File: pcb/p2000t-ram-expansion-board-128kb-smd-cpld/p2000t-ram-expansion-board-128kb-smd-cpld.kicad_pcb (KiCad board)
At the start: 2 copper layers, 110 x 45.5 mm, 14 parts, among them J1 EXPANSION BOARD, J2 POWER, J3 TERMINAL, U1 ATF1502ASV-xAx44, U2 62128

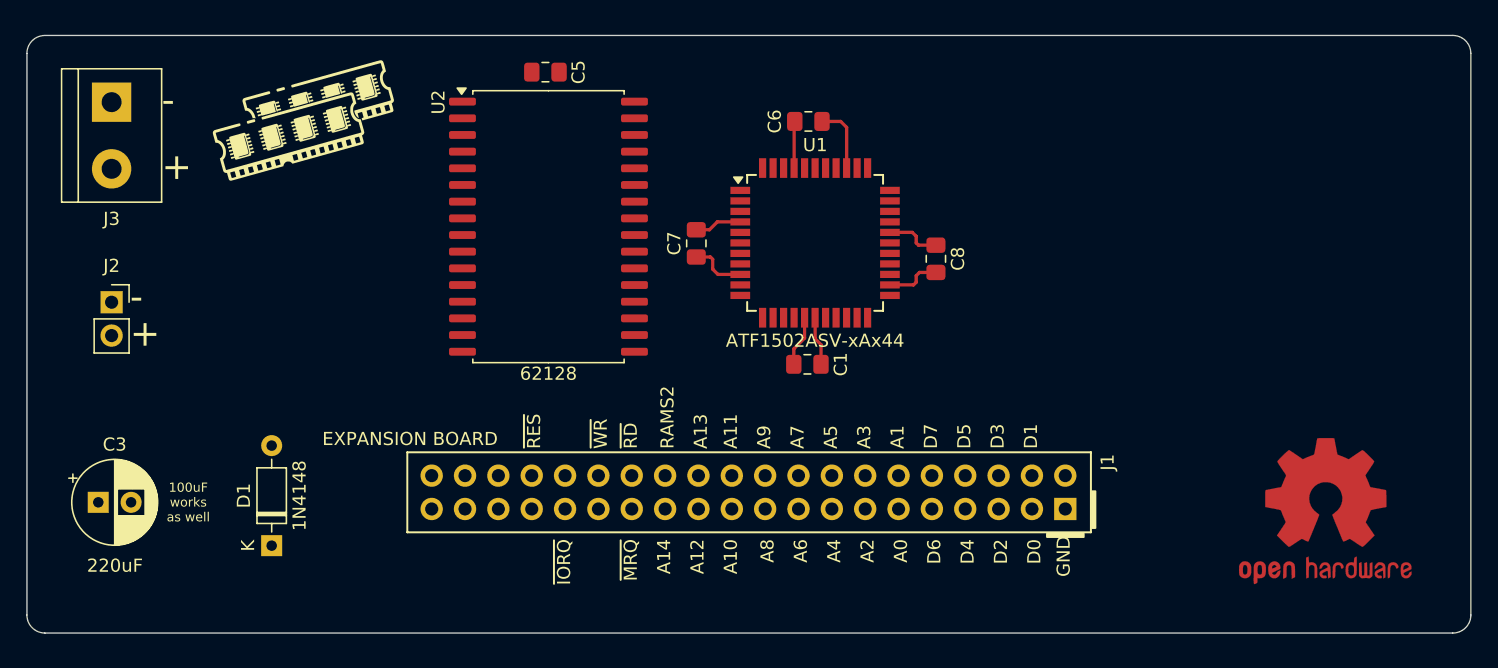
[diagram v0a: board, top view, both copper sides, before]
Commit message: Initial commit CPLD-based RAM expansion
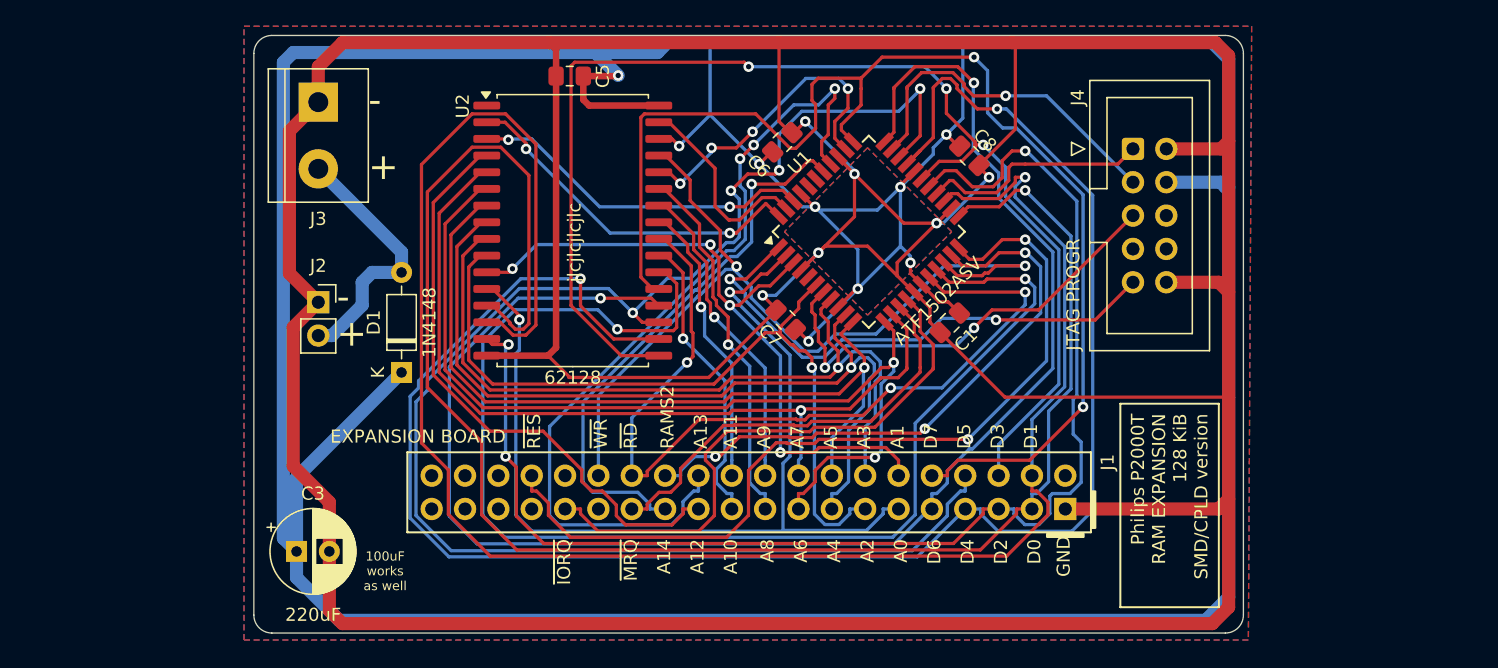
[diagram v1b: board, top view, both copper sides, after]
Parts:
- removed LOGO1: OSHW-Logo2_14.6x12mm_Copper_AND_Mask, components:OSHW-Logo2_14.6x12mm_Copper_AND_Mask
- added J4: Atmel-JTAG-10, Connector_IDC:IDC-Header_2x05_P2.54mm_Vertical, F.Cu at (104.2, 53.1)
- G***: moved to B.Cu
- U1: value ATF1502ASV-xAx44 -> ATF1502ASV
- moved G*** 20.8 mm to (61.5, 54.8), turned to 180 degrees
- moved D1 16.5 mm to (48.5, 70.1)
- moved J2 15.7 mm to (42.2, 64.8)
- moved J3 15.7 mm to (42.2, 49.5)
- moved C3 15.6 mm to (40.5, 83.8)
- moved C1 11.3 mm to (90.3, 66.3), turned to -135 degrees
- moved C7 8.96 mm to (77.8, 66.1), turned to 135 degrees
- moved C8 8.25 mm to (91.8, 53.6), turned to -45 degrees
- moved U1 4.18 mm to (84.1, 59.4), turned to 45 degrees
- moved C6 2.54 mm to (77.5, 52.6), turned to 45 degrees
- moved U2 1.87 mm to (61.5, 59.3)
- moved C5 1.87 mm to (61.3, 47.5)
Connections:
- U1 pad 1: unconnected-(U1-I/O/TDI-Pad1) -> TDI
- U1 pad 19: unconnected-(U1-I/O/PD2-Pad19) -> ~{CS1}
- U1 pad 26: unconnected-(U1-I/O/TCK-Pad26) -> TCK
- U1 pad 32: unconnected-(U1-I/O/TDO-Pad32) -> TDO
- U1 pad 35: unconnected-(U1-I/O/GCLK3-Pad35) -> R0
- U1 pad 37: unconnected-(U1-I/GCLK1-Pad37) -> A13
- U1 pad 38: unconnected-(U1-I/OE1/Vpp-Pad38) -> A14
- U1 pad 42: unconnected-(U1-I/O-Pad42) -> R1
- U1 pad 43: unconnected-(U1-I/O-Pad43) -> R2
- U1 pad 44: unconnected-(U1-I/O-Pad44) -> R3
- U1 pad 7: unconnected-(U1-I/O/TMS-Pad7) -> TMS
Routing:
- net GND: track 16.8 -> 400.2 mm, vias 0 -> 6
- net +5V: track 15.8 -> 342.9 mm, vias 0 -> 9
- net D1: track 0.00 -> 142.5 mm, vias 0 -> 1
- net D4: track 0.00 -> 140.0 mm, vias 0 -> 2
- net D0: track 0.00 -> 129.4 mm, vias 0 -> 1
- net D6: track 0.00 -> 119.5 mm, vias 0 -> 2
- net D5: track 0.00 -> 118.2 mm, vias 0 -> 4
- net D2: track 0.00 -> 100.8 mm, vias 0 -> 3
- net ~{CS1}: track 0.00 -> 98.5 mm, vias 0 -> 2
- net D3: track 0.00 -> 96.6 mm, vias 0 -> 3
- net D7: track 0.00 -> 96.1 mm, vias 0 -> 2
- net A0: track 0.00 -> 75.0 mm, vias 0 -> 2
- net A6: track 0.00 -> 72.0 mm, vias 0 -> 2
- net ~{WR}: track 0.00 -> 66.8 mm, vias 0 -> 2
- net ~{RES}: track 0.00 -> 66.1 mm, vias 0 -> 2
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- added copper zone on B.Cu, net +5V
- added copper zone on F.Cu, net GND
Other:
- board size 110 x 45.5 mm -> 75.4 x 45.5 mm
- board text added: "JTAG PROGR"
- board text added: "Philips P2000T MEMORY EXPANSION 128 KiB SMD/CPLD"
- board text added: "Philips P2000T RAM EXPANSION 128 KiB SMD/CPLD version"
- board text added: "https://github.com/ifilot/p2000t-ram-expansion-board"
